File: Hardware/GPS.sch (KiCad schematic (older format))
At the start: 10 parts

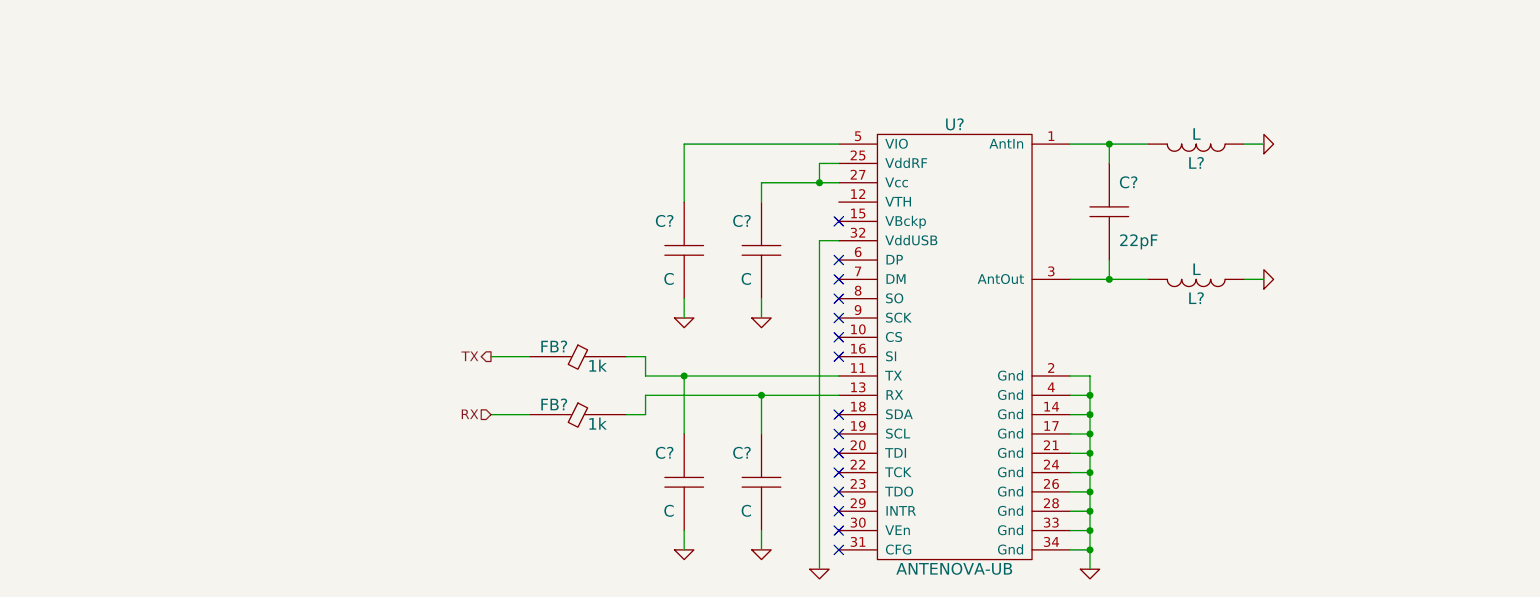
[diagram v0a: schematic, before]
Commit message: More schematic layout
GPS mostly finished
Additional transmitter layout
Core added
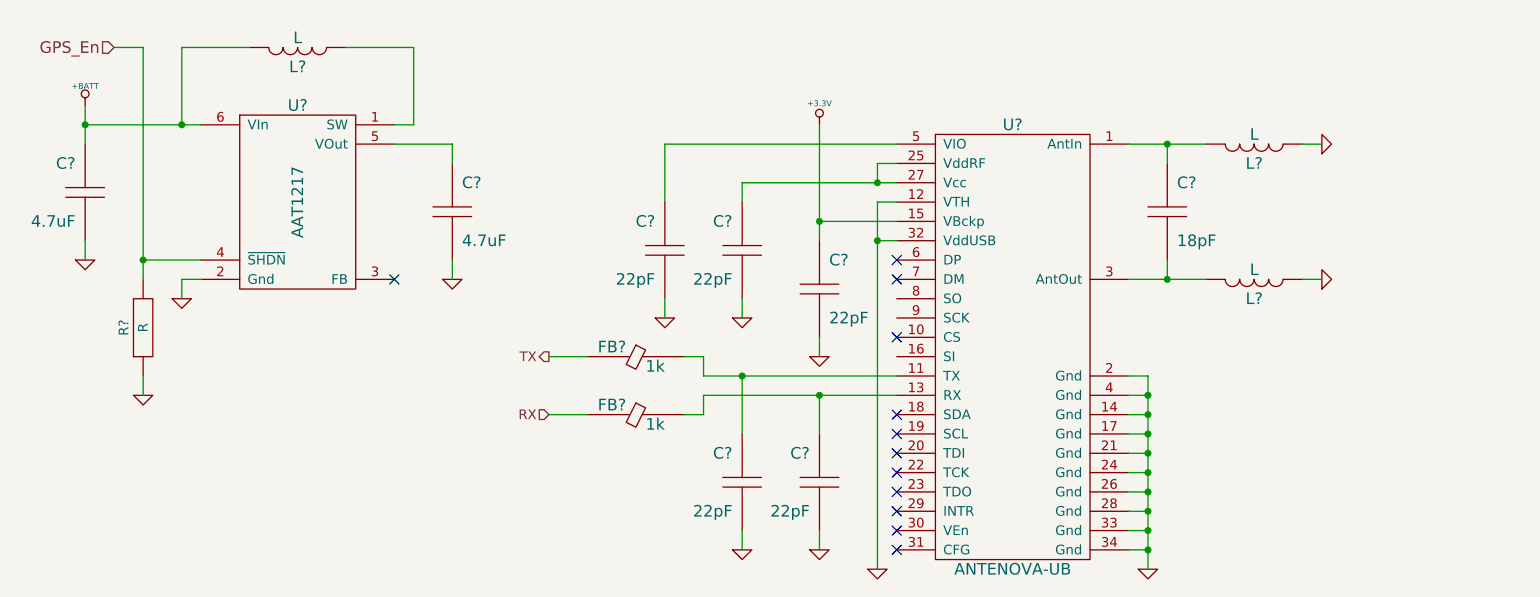
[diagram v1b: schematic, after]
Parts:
- added C? (x2): 4.7uF, ~, symbol C
- added C?: 22pF, ~, symbol C
- added L?: L, ~, symbol L
- added R?: R, ~, symbol R
- added U?: AAT1217, symbol AAT1217
- C?: value 22pF -> 18pF
- C? (x4): value C -> 22pF
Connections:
- net GND: now also U?.12 (VTH), C?.2, C?.2, C?.2, R?.1, U?.2 (Gnd)
- net +3.3V: now reaches U?.15 (VBckp)
- net +3.3V: now also C?.1
- new net: L?.2, U?.1 (SW)
- new net: C?.1, U?.5 (VOut)
- new net +BATT: C?.1, L?.1, U?.6 (VIn)
- new net GPS_En: R?.2, U?.4 (~SHDN)
- no-connect marks 15 -> 12
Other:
- moved on the sheet: C?, FB?, L?, U?

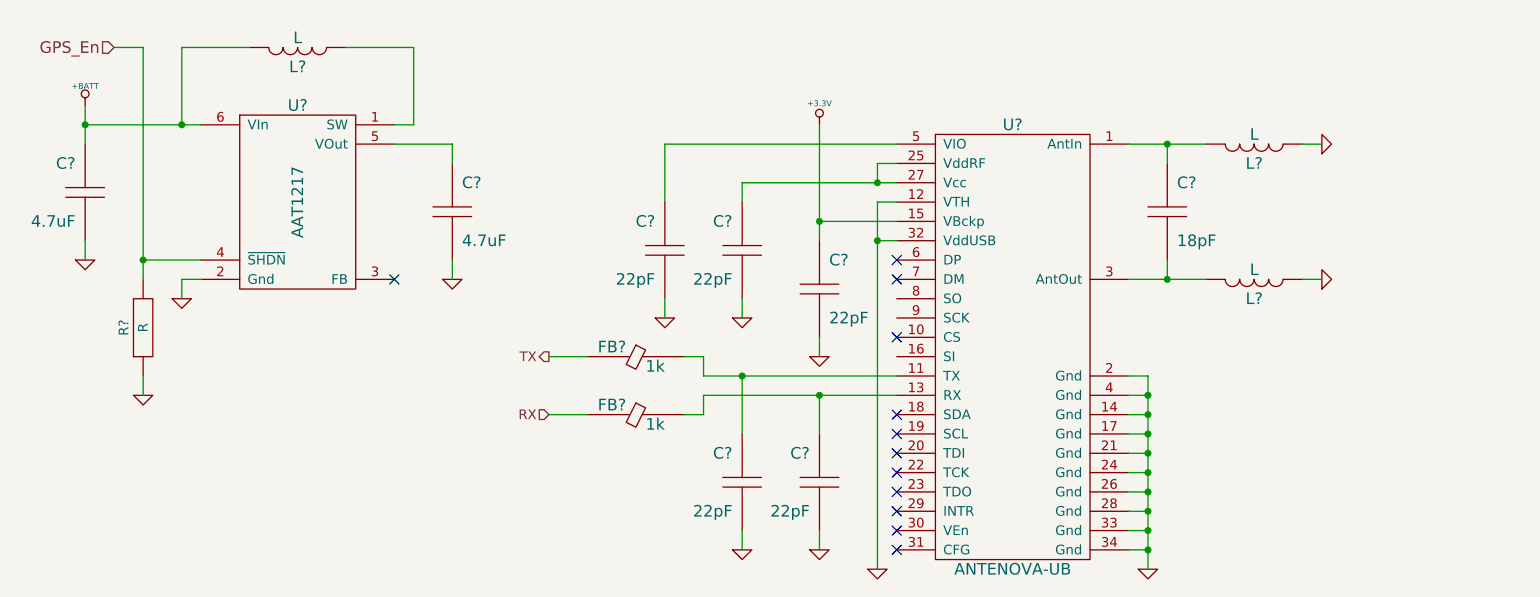
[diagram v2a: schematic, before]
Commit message: Add GPS performance control
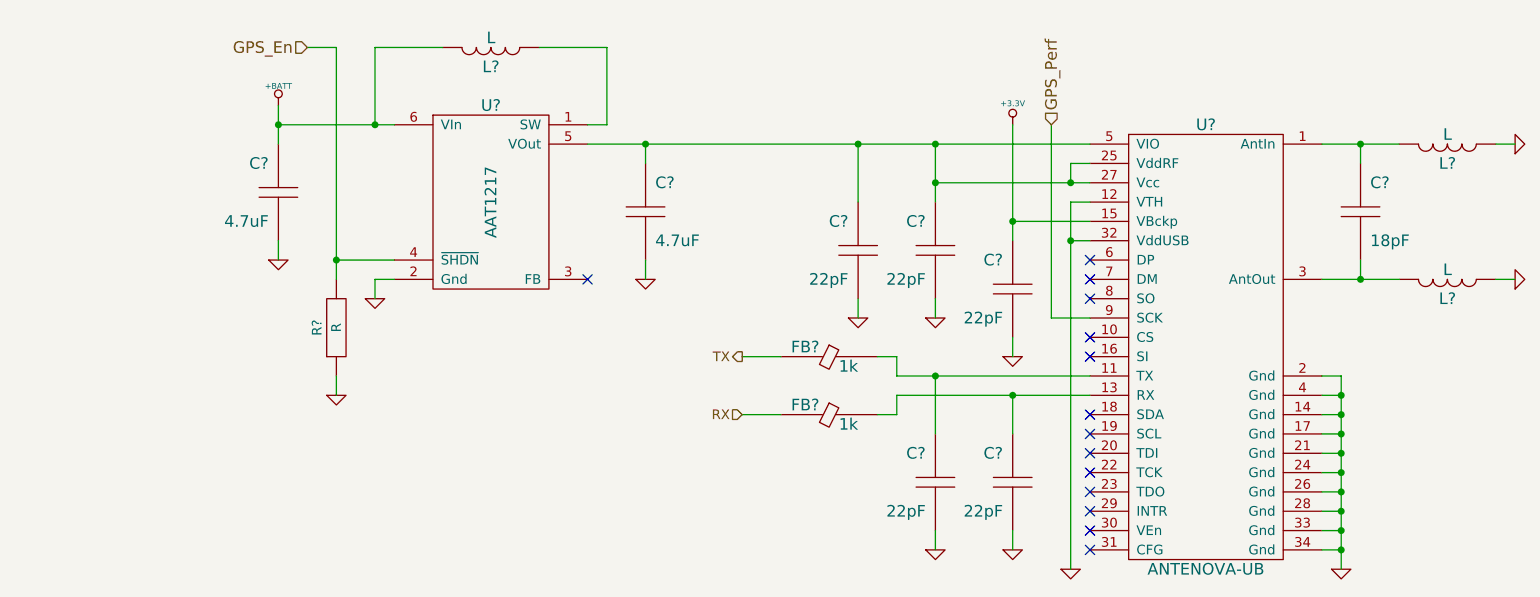
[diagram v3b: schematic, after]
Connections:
- net at C?.1, U?.25 (VddRF), U?.27 (Vcc): now also C?.1, C?.1, U?.5 (VIO), U?.5 (VOut)
- net GPS_Perf: now reaches U?.9 (SCK)
- no-connect marks 12 -> 14
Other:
- moved on the sheet: C?, FB?, L?, R?, U?

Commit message: Switch GPS power to main 3v3 bus
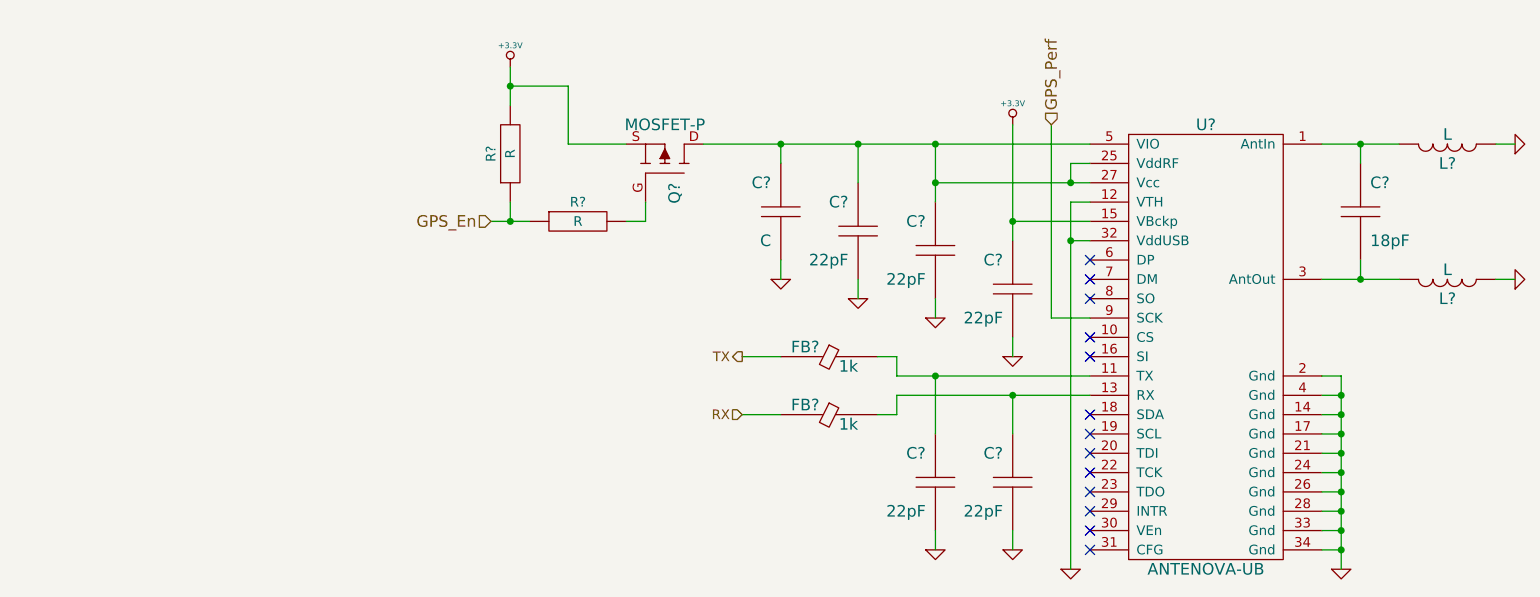
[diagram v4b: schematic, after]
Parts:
- removed C? (x2): 4.7uF, ~, symbol C
- removed L?: L, ~, symbol L
- removed R?: R, ~, symbol R
- removed U?: AAT1217, symbol AAT1217
- added C?: C, ~, symbol C
- added Q?: MOSFET-P, ~, symbol MOSFET-P
- added R? (x2): R, ~, symbol R
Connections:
- net +3.3V: now also Q?.S, R?.2
- net GND: now also C?.2
- net GPS_En: now also R?.1, R?.1
- net at C?.1, C?.1, U?.25 (VddRF)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: now also C?.1, Q?.D
- new net: Q?.G, R?.2
- no-connect marks 14 -> 13
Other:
- moved on the sheet: C?
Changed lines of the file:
@@
 Sheet 2 4
 Title "Aether - Pico Tracker"
-Date "2 feb 2014"
+Date "3 feb 2014"
 Rev "1"
 Comp "Aerodyne Labs"
@@
 	5500 4400 6500 4400
 Wire Wire Line
-	5700 3100 5700 3400
-Wire Wire Line
-	5700 3300 6500 3300
-Wire Wire Line
 	6500 3200 6400 3200
 Wire Wire Line
@@
 L C C?
 U 1 1 52E9B693
-P 5300 3650
-F 0 "C?" H 5350 3800 60  0000 L CNN
-F 1 "22pF" H 5350 3500 60  0000 L CNN
-F 2 "~" H 5300 3650 60  0000 C CNN
-F 3 "~" H 5300 3650 60  0000 C CNN
-F 4 "V" H 5250 3500 60  0001 R CNN "Voltage"
-F 5 "D" H 5250 3800 60  0001 R CNN "Dielectric"
-	1    5300 3650
-	-1   0    0    -1
-$EndComp
-Wire Wire Line
-	5300 3400 5300 3100
-Wire Wire Line
-	3900 3100 6500 3100
+P 5300 3550
+F 0 "C?" H 5350 3700 60  0000 L CNN
+F 1 "22pF" H 5350 3400 60  0000 L CNN
+F 2 "~" H 5300 3550 60  0000 C CNN
+F 3 "~" H 5300 3550 60  0000 C CNN
+F 4 "V" H 5250 3400 60  0001 R CNN "Voltage"
+F 5 "D" H 5250 3700 60  0001 R CNN "Dielectric"
+	1    5300 3550
+	-1   0    0    -1
+$EndComp
 NoConn ~ 6500 4100
 NoConn ~ 6500 4500
@@
 L GND #PWR?
 U 1 1 52E9B84B
-P 5300 4000
-F 0 "#PWR?" H 5300 4000 30  0001 C CNN
-F 1 "GND" H 5300 3930 30  0001 C CNN
-F 2 "" H 5300 4000 60  0000 C CNN
-F 3 "" H 5300 4000 60  0000 C CNN
-	1    5300 4000
-	1    0    0    -1
-$EndComp
-Wire Wire Line
-	5300 4000 5300 3900
+P 5300 3900
+F 0 "#PWR?" H 5300 3900 30  0001 C CNN
+F 1 "GND" H 5300 3830 30  0001 C CNN
+F 2 "" H 5300 3900 60  0000 C CNN
+F 3 "" H 5300 3900 60  0000 C CNN
+	1    5300 3900
+	1    0    0    -1
+$EndComp
+Wire Wire Line
+	5300 3900 5300 3800
 Wire Wire Line
 	5700 3900 5700 4000
@@
 NoConn ~ 6500 4700
 NoConn ~ 6500 5200
-$Comp
-L AAT1217 U?
-U 1 1 52ECD028
-P 3400 3400
-F 0 "U?" H 3400 3900 60  0000 C CNN
-F 1 "AAT1217" V 3400 3400 60  0000 C CNN
-F 2 "" H 3400 3400 60  0000 C CNN
-F 3 "" H 3400 3400 60  0000 C CNN
-	1    3400 3400
-	1    0    0    -1
-$EndComp
-$Comp
-L C C?
-U 1 1 52ECD037
-P 4200 3450
-F 0 "C?" H 4250 3600 60  0000 L CNN
-F 1 "4.7uF" H 4250 3300 60  0000 L CNN
-F 2 "~" H 4200 3450 60  0000 C CNN
-F 3 "~" H 4200 3450 60  0000 C CNN
-F 4 "V" H 4150 3300 60  0001 R CNN "Voltage"
-F 5 "D" H 4150 3600 60  0001 R CNN "Dielectric"
-	1    4200 3450
-	1    0    0    -1
-$EndComp
-$Comp
-L L L?
-U 1 1 52ECD059
-P 3400 2600
-F 0 "L?" H 3400 2500 60  0000 C CNN
-F 1 "L" H 3400 2650 60  0000 C CNN
-F 2 "~" H 3400 2600 60  0000 C CNN
-F 3 "~" H 3400 2600 60  0000 C CNN
-	1    3400 2600
-	1    0    0    -1
-$EndComp
-Wire Wire Line
-	3650 2600 4000 2600
-Wire Wire Line
-	4000 2600 4000 3000
-Wire Wire Line
-	4000 3000 3900 3000
-$Comp
-L C C?
-U 1 1 52ECD0A1
-P 2300 3350
-F 0 "C?" H 2350 3500 60  0000 L CNN
-F 1 "4.7uF" H 2350 3200 60  0000 L CNN
-F 2 "~" H 2300 3350 60  0000 C CNN
-F 3 "~" H 2300 3350 60  0000 C CNN
-F 4 "V" H 2250 3200 60  0001 R CNN "Voltage"
-F 5 "D" H 2250 3500 60  0001 R CNN "Dielectric"
-	1    2300 3350
-	-1   0    0    -1
-$EndComp
-$Comp
-L +BATT #PWR?
-U 1 1 52ECD0BC
-P 2300 2900
-F 0 "#PWR?" H 2300 2850 20  0001 C CNN
-F 1 "+BATT" H 2300 3000 30  0000 C CNN
-F 2 "" H 2300 2900 60  0000 C CNN
-F 3 "" H 2300 2900 60  0000 C CNN
-	1    2300 2900
-	1    0    0    -1
-$EndComp
-Wire Wire Line
-	2300 2900 2300 3100
-Wire Wire Line
-	2300 3000 2900 3000
-Connection ~ 2300 3000
-Wire Wire Line
-	3150 2600 2800 2600
-Wire Wire Line
-	2800 2600 2800 3000
-Connection ~ 2800 3000
-Wire Wire Line
-	4200 3100 4200 3200
-$Comp
-L GND #PWR?
-U 1 1 52ECD1D9
-P 4200 3800
-F 0 "#PWR?" H 4200 3800 30  0001 C CNN
-F 1 "GND" H 4200 3730 30  0001 C CNN
-F 2 "" H 4200 3800 60  0000 C CNN
-F 3 "" H 4200 3800 60  0000 C CNN
-	1    4200 3800
-	1    0    0    -1
-$EndComp
-NoConn ~ 3900 3800
-Wire Wire Line
-	4200 3700 4200 3800
-$Comp
-L GND #PWR?
-U 1 1 52ECD24D
-P 2800 3900
-F 0 "#PWR?" H 2800 3900 30  0001 C CNN
-F 1 "GND" H 2800 3830 30  0001 C CNN
-F 2 "" H 2800 3900 60  0000 C CNN
-F 3 "" H 2800 3900 60  0000 C CNN
-	1    2800 3900
-	1    0    0    -1
-$EndComp
-Wire Wire Line
-	2900 3800 2800 3800
-Wire Wire Line
-	2800 3800 2800 3900
-$Comp
-L GND #PWR?
-U 1 1 52ECD2A0
-P 2300 3700
-F 0 "#PWR?" H 2300 3700 30  0001 C CNN
-F 1 "GND" H 2300 3630 30  0001 C CNN
-F 2 "" H 2300 3700 60  0000 C CNN
-F 3 "" H 2300 3700 60  0000 C CNN
-	1    2300 3700
-	1    0    0    -1
-$EndComp
-Wire Wire Line
-	2300 3700 2300 3600
-Text HLabel 2450 2600 0    60   Input ~ 0
+Text HLabel 3400 3500 0    60   Input ~ 0
 GPS_En
-$Comp
-L R R?
-U 1 1 52ECD3F8
-P 2600 4050
-F 0 "R?" H 2600 4150 50  0000 C CNN
-F 1 "R" H 2600 4050 50  0000 C CNN
-F 2 "~" H 2600 4050 60  0000 C CNN
-F 3 "~" H 2600 4050 60  0000 C CNN
-F 4 "W" H 2600 3950 50  0001 C CNN "Power"
-F 5 "%" H 2600 3850 50  0001 C CNN "Tolerance"
-	1    2600 4050
-	0    -1   -1   0
-$EndComp
-$Comp
-L GND #PWR?
-U 1 1 52ECD413
-P 2600 4400
-F 0 "#PWR?" H 2600 4400 30  0001 C CNN
-F 1 "GND" H 2600 4330 30  0001 C CNN
-F 2 "" H 2600 4400 60  0000 C CNN
-F 3 "" H 2600 4400 60  0000 C CNN
-	1    2600 4400
-	1    0    0    -1
-$EndComp
-Wire Wire Line
-	2600 4300 2600 4400
-Wire Wire Line
-	2450 2600 2600 2600
-Wire Wire Line
-	2600 2600 2600 3800
-Wire Wire Line
-	2900 3700 2600 3700
-Connection ~ 2600 3700
 $Comp
 L C C?
@@
 Wire Wire Line
 	6300 4000 6500 4000
+Wire Wire Line
+	5700 3300 6500 3300
+Wire Wire Line
+	5700 3100 5700 3400
+Wire Wire Line
+	4500 3100 6500 3100
+Wire Wire Line
+	5300 3100 5300 3300
+$Comp
+L MOSFET-P Q?
+U 1 1 52EF2A40
+P 4300 3200
+F 0 "Q?" H 4200 3150 60  0000 R CNN
+F 1 "MOSFET-P" V 4500 3200 60  0000 C CNN
+F 2 "~" H 4300 3200 60  0000 C CNN
+F 3 "~" H 4300 3200 60  0000 C CNN
+	1    4300 3200
+	0    -1   -1   0
+$EndComp
+$Comp
+L R R?
+U 1 1 52EF2A4F
+P 3850 3500
+F 0 "R?" H 3850 3600 50  0000 C CNN
+F 1 "R" H 3850 3500 50  0000 C CNN
+F 2 "~" H 3850 3500 60  0000 C CNN
+F 3 "~" H 3850 3500 60  0000 C CNN
+F 4 "W" H 3850 3400 50  0001 C CNN "Power"
+F 5 "%" H 3850 3300 50  0001 C CNN "Tolerance"
+	1    3850 3500
+	1    0    0    -1
+$EndComp
+$Comp
+L C C?
+U 1 1 52EF2A6A
+P 4900 3450
+F 0 "C?" H 4950 3600 60  0000 L CNN
+F 1 "C" H 4950 3300 60  0000 L CNN
+F 2 "~" H 4900 3450 60  0000 C CNN
+F 3 "~" H 4900 3450 60  0000 C CNN
+F 4 "V" H 4850 3300 60  0001 R CNN "Voltage"
+F 5 "D" H 4850 3600 60  0001 R CNN "Dielectric"
+	1    4900 3450
+	-1   0    0    -1
+$EndComp
+$Comp
+L GND #PWR?
+U 1 1 52EF2A9A
+P 4900 3800
+F 0 "#PWR?" H 4900 3800 30  0001 C CNN
+F 1 "GND" H 4900 3730 30  0001 C CNN
+F 2 "" H 4900 3800 60  0000 C CNN
+F 3 "" H 4900 3800 60  0000 C CNN
+	1    4900 3800
+	1    0    0    -1
+$EndComp
+Wire Wire Line
+	4900 3800 4900 3700
 Connection ~ 5300 3100
-Connection ~ 4200 3100
 Connection ~ 5700 3100
 Connection ~ 5700 3300
+Wire Wire Line
+	4900 3200 4900 3100
+Connection ~ 4900 3100
+Wire Wire Line
+	4200 3400 4200 3500
+Wire Wire Line
+	4200 3500 4100 3500
+$Comp
+L R R?
+U 1 1 52EF2C24
+P 3500 3150
+F 0 "R?" H 3500 3250 50  0000 C CNN
+F 1 "R" H 3500 3150 50  0000 C CNN
+F 2 "~" H 3500 3150 60  0000 C CNN
+F 3 "~" H 3500 3150 60  0000 C CNN
+F 4 "W" H 3500 3050 50  0001 C CNN "Power"
+F 5 "%" H 3500 2950 50  0001 C CNN "Tolerance"
+	1    3500 3150
+	0    -1   -1   0
+$EndComp
+Wire Wire Line
+	3400 3500 3600 3500
+Wire Wire Line
+	3500 3400 3500 3500
+Connection ~ 3500 3500
+$Comp
+L +3.3V #PWR?
+U 1 1 52EF2CCE
+P 3500 2700
+F 0 "#PWR?" H 3500 2660 30  0001 C CNN
+F 1 "+3.3V" H 3500 2810 30  0000 C CNN
+F 2 "" H 3500 2700 60  0000 C CNN
+F 3 "" H 3500 2700 60  0000 C CNN
+	1    3500 2700
+	1    0    0    -1
+$EndComp
+Wire Wire Line
+	3500 2700 3500 2900
+Wire Wire Line
+	3500 2800 3800 2800
+Wire Wire Line
+	3800 2800 3800 3100
+Wire Wire Line
+	3800 3100 4100 3100
+Connection ~ 3500 2800
 $EndSCHEMATC
